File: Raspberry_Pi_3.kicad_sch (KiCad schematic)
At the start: 2 parts, among them J1 Raspberry_Pi_2_3, U5 Fe-Pi_V2

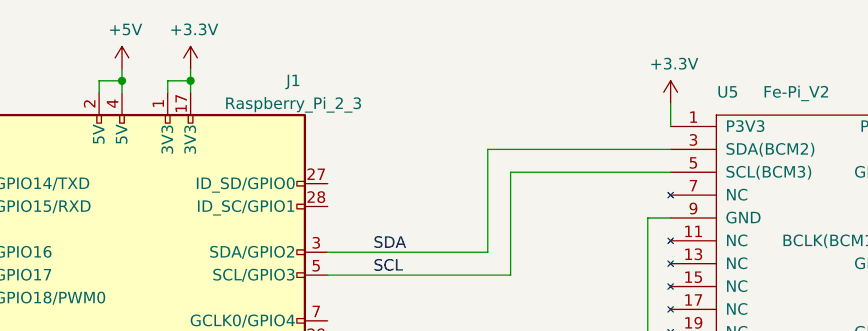
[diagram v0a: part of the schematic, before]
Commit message: update to Kicad v9
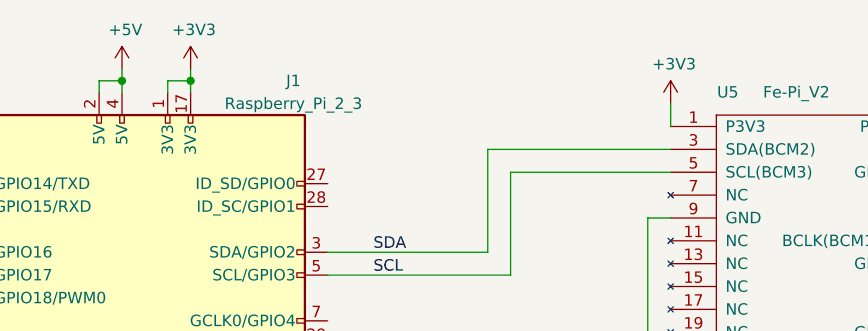
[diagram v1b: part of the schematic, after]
